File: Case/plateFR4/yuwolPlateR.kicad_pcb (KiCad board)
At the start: 2 copper layers, 173.5 x 126 mm, 1 part

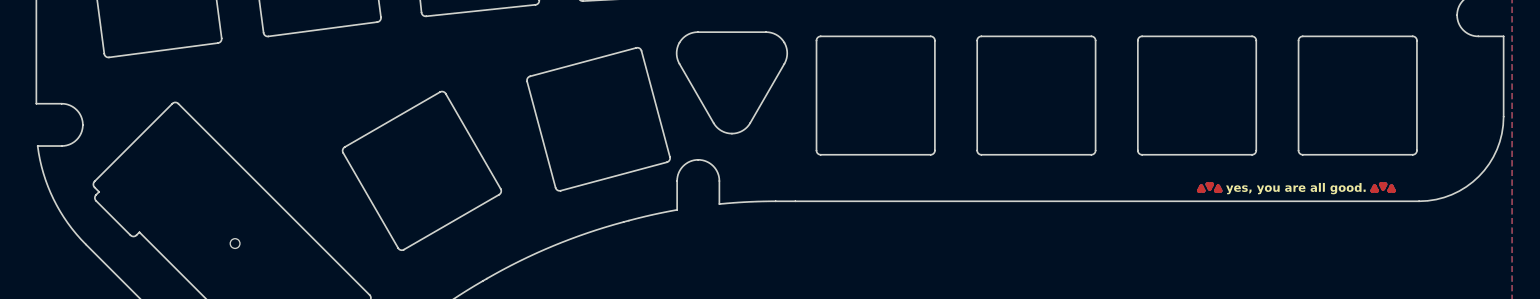
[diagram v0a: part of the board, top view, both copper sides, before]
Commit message: change plate gerber hole to via
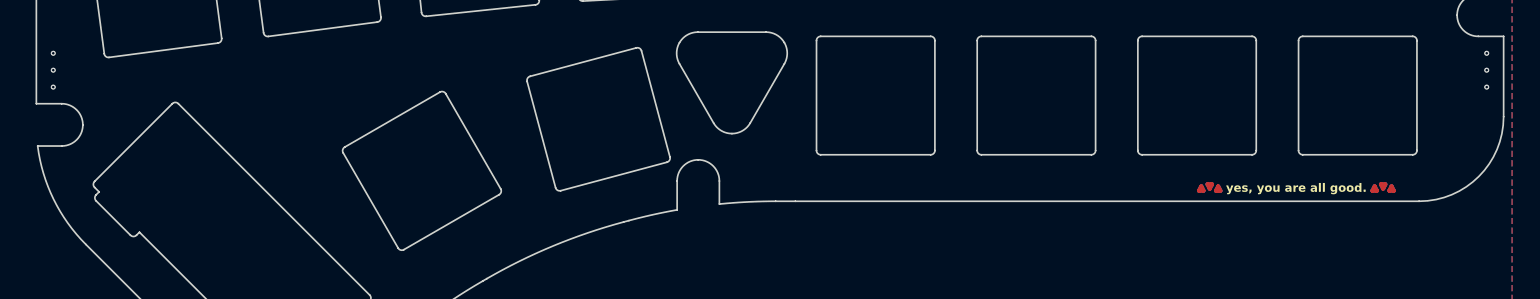
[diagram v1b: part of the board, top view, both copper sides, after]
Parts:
- removed REF**: ToolingHole_1.152mm, MountingHole:ToolingHole_1.152mm
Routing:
- net GND: vias 0 -> 6
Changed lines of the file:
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@@
 		(capping no)
 		(filling no)
+		(zone_defaults)
 		(pcbplotparams
 			(layerselection 0x00000000_00000000_55555555_5755f5ff)
@@
 		)
 	)
-	(footprint "MountingHole:ToolingHole_1.152mm"
-		(layer "F.Cu")
-		(at 84 142)
-		(descr "Tooling Hole 1.152mm, 1.3mm solder mask, JLCPCB specification, https://jlcpcb.com/help/article/How-to-add-tooling-holes-for-PCB-assembly-order")
-		(tags "mounting")
-		(property "Reference" "REF**"
-			(at 0 -1.5 0)
-			(layer "F.SilkS")
-			(hide yes)
-			(effects
-				(font
-					(size 1 1)
-					(thickness 0.15)
-				)
-			)
-		)
-		(property "Value" "ToolingHole_1.152mm"
-			(at 0 1.6 0)
-			(layer "F.Fab")
-			(effects
-				(font
-					(size 1 1)
-					(thickness 0.15)
-				)
-			)
-		)
-		(property "Datasheet" ""
-			(at 0 0 0)
-			(unlocked yes)
-			(layer "F.Fab")
-			(hide yes)
-			(effects
-				(font
-					(size 1.27 1.27)
-					(thickness 0.15)
-				)
-			)
-		)
-		(property "Description" ""
-			(at 0 0 0)
-			(unlocked yes)
-			(layer "F.Fab")
-			(hide yes)
-			(effects
-				(font
-					(size 1.27 1.27)
-					(thickness 0.15)
-				)
-			)
-		)
-		(attr exclude_from_pos_files exclude_from_bom)
-		(duplicate_pad_numbers_are_jumpers no)
-		(fp_circle
-			(center 0 0)
-			(end 0.7 0)
-			(stroke
-				(width 0.05)
-				(type solid)
-			)
-			(fill no)
-			(layer "F.CrtYd")
-		)
-		(fp_text user "${REFERENCE}"
-			(at 0 0 0)
-			(layer "F.Fab")
-			(effects
-				(font
-					(size 1 1)
-					(thickness 0.15)
-				)
-			)
-		)
-		(pad "" np_thru_hole circle
-			(at 0 0)
-			(size 1.152 1.152)
-			(drill 1.152)
-			(layers "*.Cu" "*.Mask")
-			(solder_mask_margin 0.074)
-		)
-		(zone
-			(layers "F.Cu" "B.Cu")
-			(hatch edge 0.5)
-			(connect_pads
-				(clearance 0)
-			)
-			(min_thickness 0.25)
-			(keepout
-				(tracks not_allowed)
-				(vias allowed)
-				(pads allowed)
-				(copperpour not_allowed)
-				(footprints not_allowed)
-			)
-			(placement
-				(enabled no)
-				(sheetname "")
-			)
-			(fill
-				(thermal_gap 0.5)
-				(thermal_bridge_width 0.5)
-				(island_removal_mode 0)
-			)
-			(polygon
-				(pts
-					(xy 84.7 142) (xy 84.679659 141.832479) (xy 84.619819 141.674694) (xy 84.523958 141.535814) (xy 84.397645 141.423911)
-					(xy 84.248223 141.345489) (xy 84.084376 141.305104) (xy 83.915624 141.305104) (xy 83.751777 141.345489)
-					(xy 83.602355 141.423911) (xy 83.476042 141.535814) (xy 83.380181 141.674694) (xy 83.320341 141.832479)
-					(xy 83.3 142) (xy 83.320341 142.167521) (xy 83.380181 142.325306) (xy 83.476042 142.464186) (xy 83.602355 142.576089)
-					(xy 83.751777 142.654511) (xy 83.915624 142.694896) (xy 84.084376 142.694896) (xy 84.248223 142.654511)
-					(xy 84.397645 142.576089) (xy 84.523958 142.464186) (xy 84.619819 142.325306) (xy 84.679659 142.167521)
-				)
-			)
-		)
-		(embedded_fonts no)
-	)
 	(gr_line
 		(start 198 135.75)
@@
 		)
 	)
+	(via
+		(at 62.5 121.5)
+		(size 0.6)
+		(drill 0.3)
+		(layers "F.Cu" "B.Cu")
+		(free yes)
+		(net "GND")
+	)
+	(via
+		(at 232 123.5)
+		(size 0.6)
+		(drill 0.3)
+		(layers "F.Cu" "B.Cu")
+		(free yes)
+		(net "GND")
+	)
+	(via
+		(at 62.5 119.5)
+		(size 0.6)
+		(drill 0.3)
+		(layers "F.Cu" "B.Cu")
+		(net "GND")
+	)
+	(via
+		(at 232 119.5)
+		(size 0.6)
+		(drill 0.3)
+		(layers "F.Cu" "B.Cu")
+		(free yes)
+		(net "GND")
+	)
+	(via
+		(at 232 121.5)
+		(size 0.6)
+		(drill 0.3)
+		(layers "F.Cu" "B.Cu")
+		(free yes)
+		(net "GND")
+	)
+	(via
+		(at 62.5 123.5)
+		(size 0.6)
+		(drill 0.3)
+		(layers "F.Cu" "B.Cu")
+		(net "GND")
+	)
 	(zone
